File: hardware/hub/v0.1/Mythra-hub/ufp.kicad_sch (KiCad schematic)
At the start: 18 parts, among them J1 918-418K2022C40000, J11 DFP SWD, U2 HD3SS460, U20 CYPD3174-24, U35 SP3400-02UTG

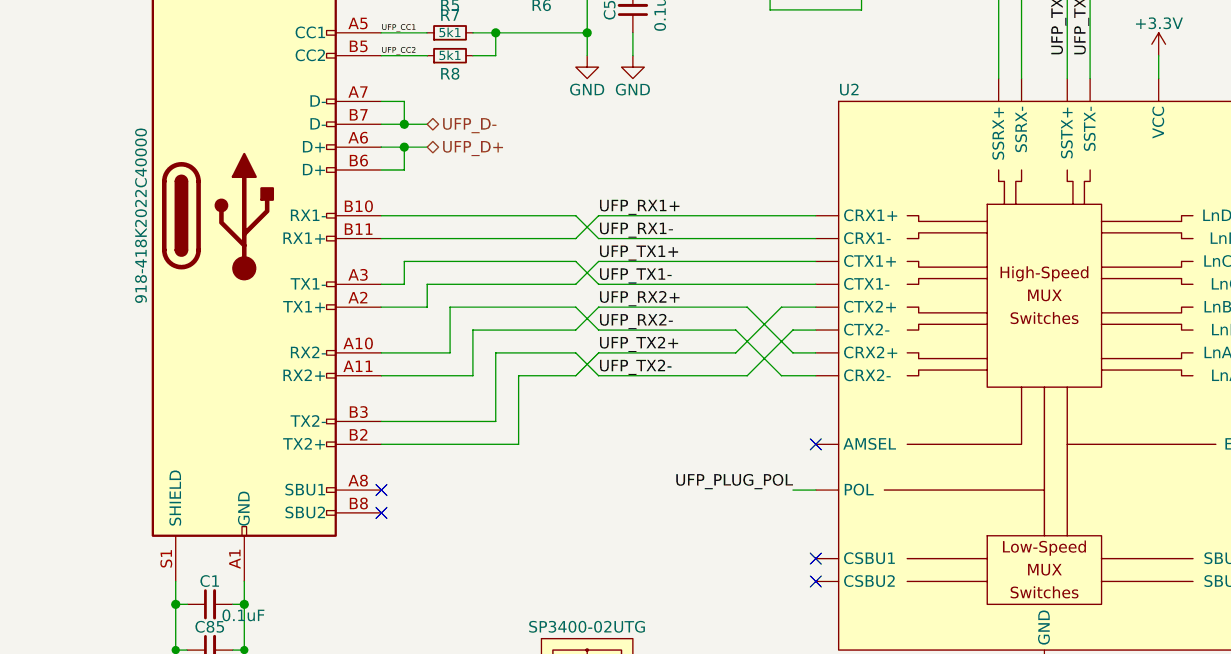
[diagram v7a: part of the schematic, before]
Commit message: Upgraded the schematic files to KiCad 6 format and done some tidy up from the manufacturing crunch
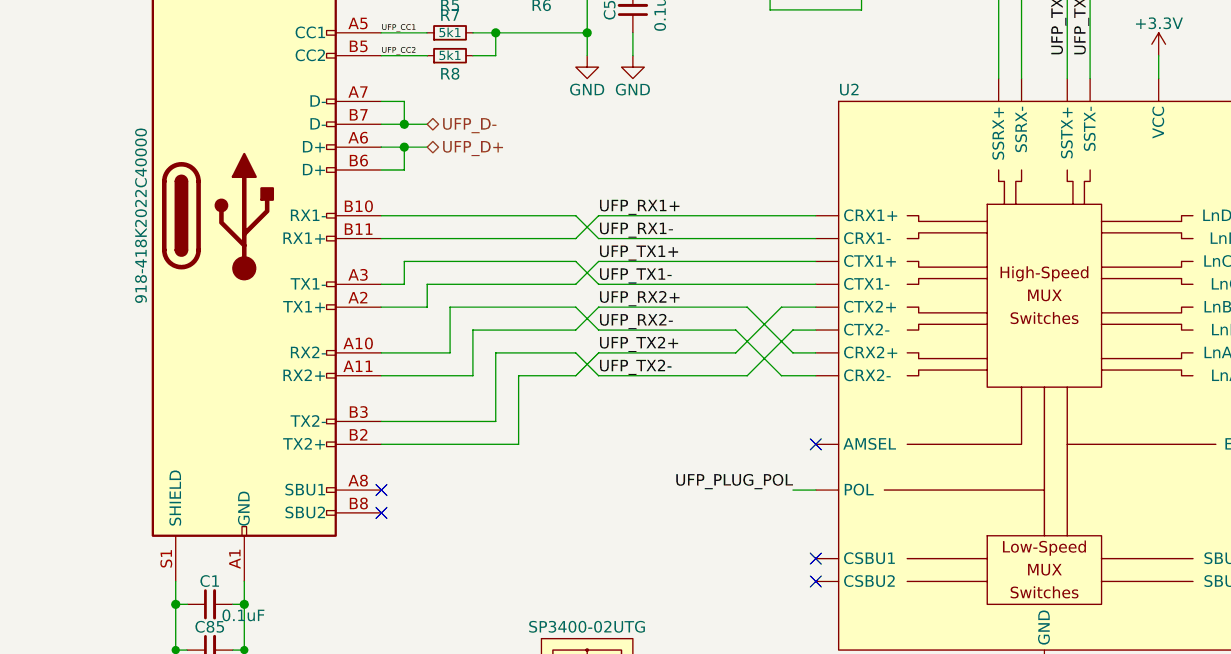
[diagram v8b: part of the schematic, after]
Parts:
- C85: MFR Yageo -> Walsin; MPN RC0402FR-0710KL -> 0402B102K500CT; OC_FARNELL (none) -> 2496767; OC_LCSC C60490 -> (none); URL_FARNELL (none) -> https://uk.farnell.com/walsin/0402b102k500ct/cap-1000pf-50v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; URL_LCSC https://www.lcsc.com/product-detail/Chip-Resistor-Surface-M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 -> (none)
